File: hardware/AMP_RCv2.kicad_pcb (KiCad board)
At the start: 2 copper layers, 100 x 85 mm, 47 parts, among them CN3 Conn_01x15, CN4 Conn_01x15, J1 USB_C_Receptacle_USB2.0_16P, SW1 SW_UP, SW2 SW_LEFT, SW3 SW_DOWN, SW4 SW_RIGHT, SW5 ON/OFF, U1 TPS61023, U2 MCP73831-2-OT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

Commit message: Finish routing
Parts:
- removed CN3, CN4: Conn_01x15, Connector_PinHeader_2.54mm:PinHeader_1x15_P2.54mm_Vertical
- added U7: NUCLEO32-F303K8, AMP_Custom:NUCLEO32, F.Cu at (145.7, 76.3)
- moved C8 142.7 mm to (167.0, 57.5), turned to 90 degrees
- moved C11 142.2 mm to (179.3, 69.5), turned to -90 degrees
- moved C12 129.8 mm to (174.8, 95.9), turned to -90 degrees
- moved C9 126.0 mm to (160.9, 63.0), turned to 180 degrees
- moved R9 124.6 mm to (181.5, 69.5), turned to -90 degrees
- moved C10 124.3 mm to (167.2, 84.3), turned to -90 degrees
- moved R6 112.8 mm to (169.2, 57.5), turned to 90 degrees
- moved R10 106.5 mm to (177.0, 95.9), turned to -90 degrees
- moved R7 97.6 mm to (160.9, 65.2), turned to 180 degrees
- moved L1 95.1 mm to (126.6, 121.0)
- moved R8 92.1 mm to (169.4, 84.3), turned to -90 degrees
- moved C4 90.7 mm to (128.7, 110.9), turned to 180 degrees
- moved C3 89.6 mm to (128.7, 113.1), turned to 180 degrees
- moved BT1 88.0 mm to (120.1, 131.2), turned to 0 degrees
- moved C7 86.0 mm to (116.0, 80.0), turned to -90 degrees
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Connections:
- net /PA7 renamed /SPI1_MOSI
- net /PB3 renamed /SPI1_SCK
- U5 pad 2: /PA6 -> /SPI1_MISO
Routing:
- net +3V3: track 0.00 -> 146.4 mm
- net /VBAT: track 0.00 -> 90.8 mm
- net /SPI1_SCK: track 0.00 -> 68.7 mm, vias 0 -> 3
- net +5V: track 0.00 -> 66.7 mm, vias 0 -> 2
- net /BAT_CHRG_STAT: track 0.00 -> 65.3 mm, vias 0 -> 6
- net /SPI1_MOSI: track 0.00 -> 64.4 mm, vias 0 -> 5
- net Net-(SW5-A): track 0.00 -> 60.3 mm
- net /JOYSTICK_RIGHT_H: track 0.00 -> 57.5 mm
- net /JOYSTICK_LEFT_V: track 0.00 -> 57.1 mm, vias 0 -> 4
- net /JOYSTICK_LEFT_H: track 0.00 -> 49.9 mm, vias 0 -> 4
- net GND: track 0.00 -> 47.3 mm, vias 0 -> 19
- net /JOYSTICK_RIGHT_V: track 0.00 -> 44.8 mm
- net /JOYSTICK_RIGHT_SW: track 0.00 -> 43.7 mm, vias 0 -> 4
- net /BUTTON_UP: track 0.00 -> 38.1 mm, vias 0 -> 2
- net /BUTTON_LEFT: track 0.00 -> 35.1 mm, vias 0 -> 2
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- added copper zone on B.Cu, net GND

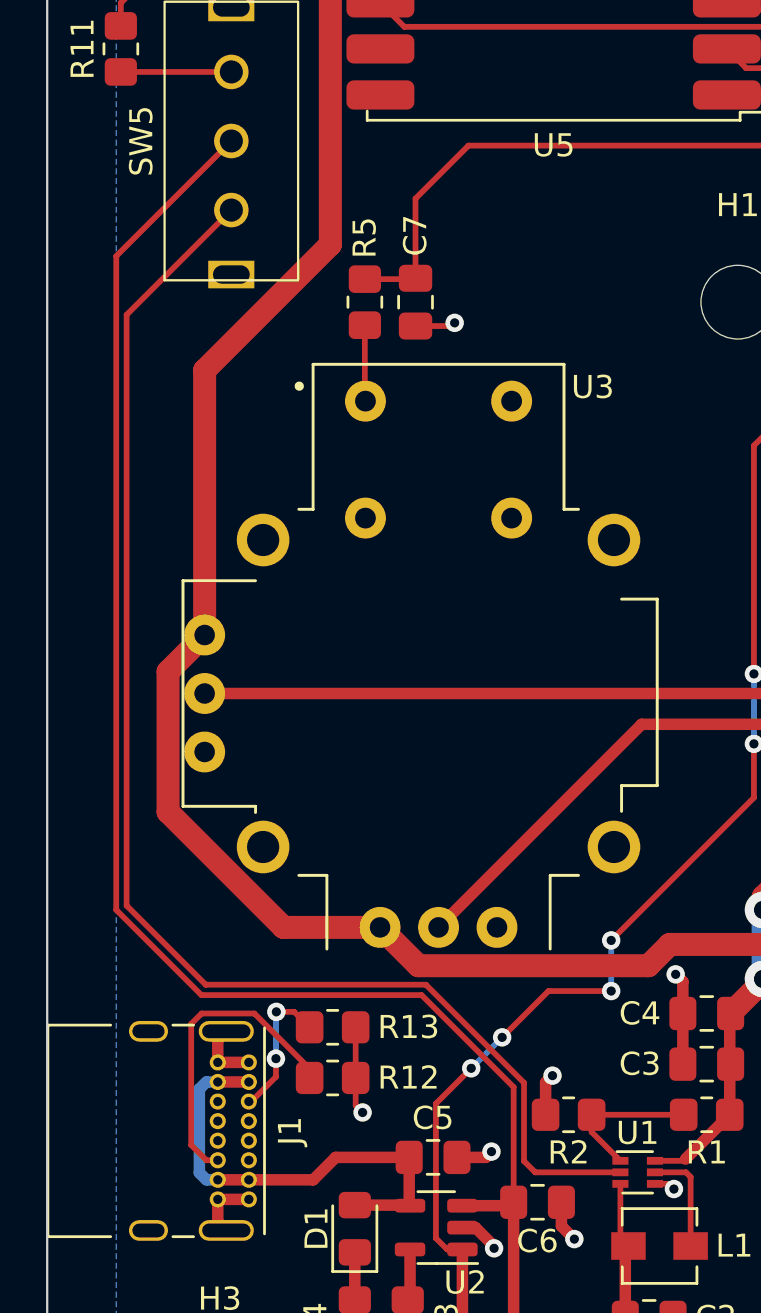
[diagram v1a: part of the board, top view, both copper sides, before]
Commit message: Fix incorrect power switch wiring
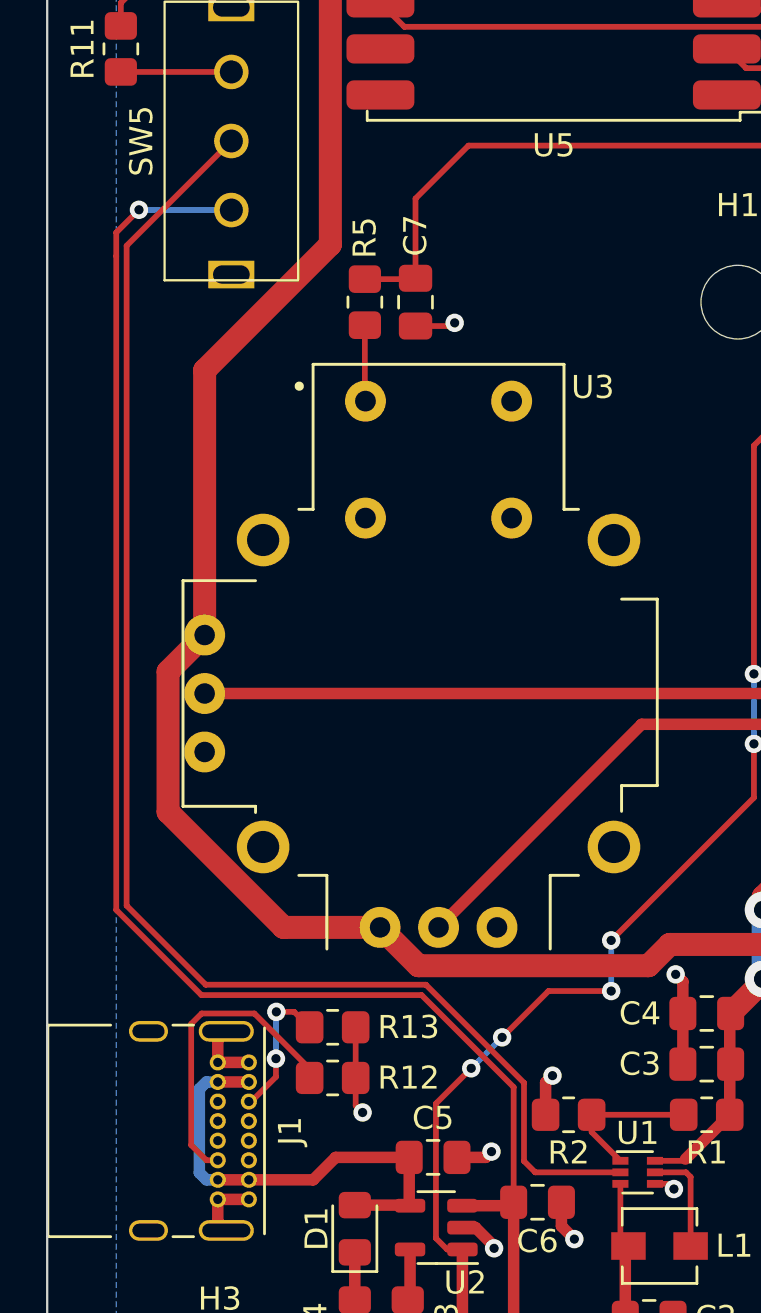
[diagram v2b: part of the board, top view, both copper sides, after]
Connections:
- SW5 pad 1: Net-(SW5-A) -> /VBAT
- SW5 pad 2: /VBAT -> Net-(SW5-B)
- U1 pad 2: Net-(SW5-A) -> Net-(SW5-B)
- U7 pad 28: unconnected-(U7-NRST-Pad28) -> unconnected-(U7-NRST-Pad28)_0
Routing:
- net Net-(SW5-B): track 0.00 -> 63.3 mm
- net Net-(SW5-A): track 60.3 -> 0.00 mm
- net /VBAT: track 90.8 -> 90.1 mm, vias 0 -> 1

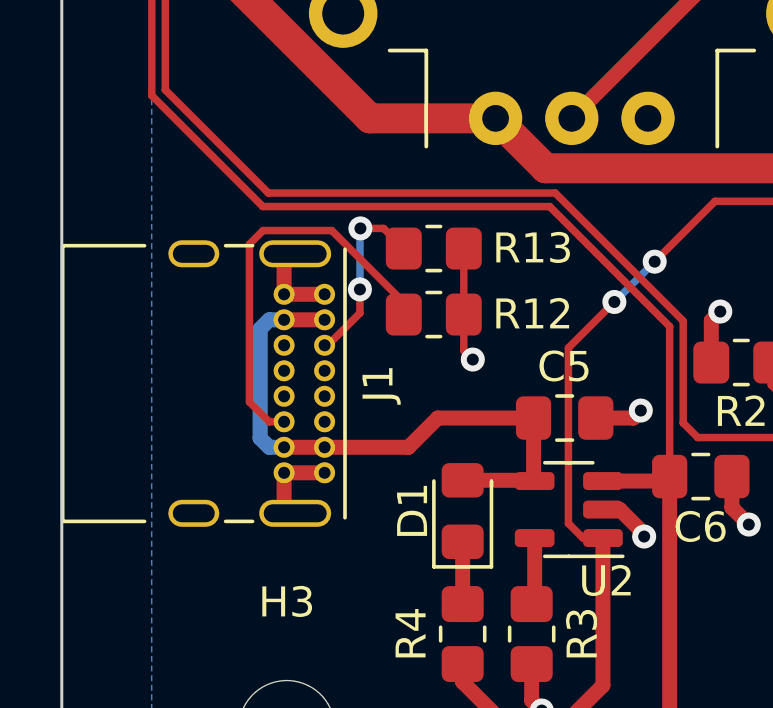
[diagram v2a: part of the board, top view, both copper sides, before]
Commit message: Replace USB-C port
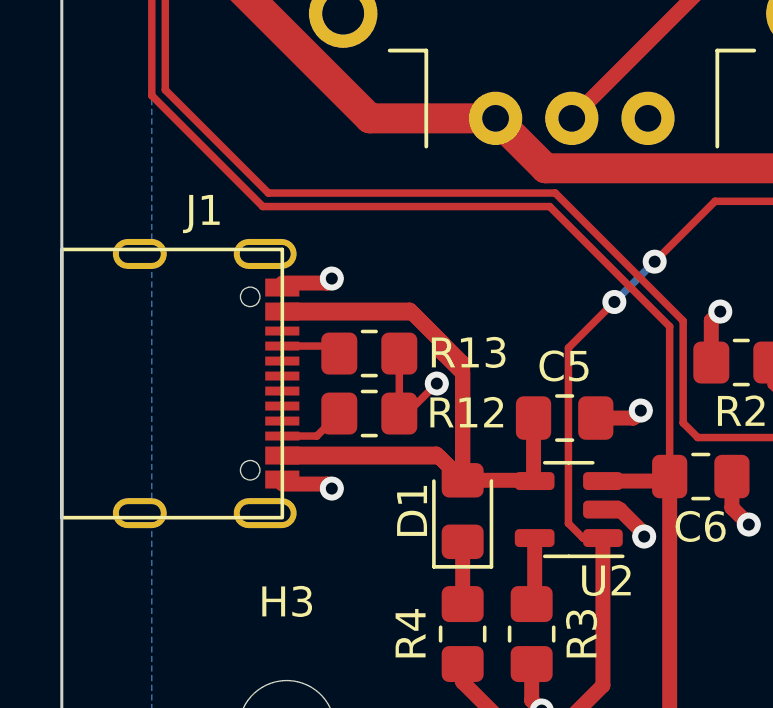
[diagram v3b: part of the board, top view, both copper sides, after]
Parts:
- J1: footprint Connector_USB:USB_C_Receptacle_GCT_USB4085 -> AMP_Custom:USB_C_Receptacle_Amphenol_C12402012
- moved J1 6.31 mm to (102.6, 111.7)
- moved R13 4.11 mm to (110.2, 115.0)
- moved R12 3.94 mm to (110.2, 117.0)
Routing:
- net VBUS: track 20.1 -> 38.4 mm
- net Net-(J1-CC2): track 13.4 -> 2.21 mm
- net Net-(J1-CC1): track 6.18 -> 2.00 mm, vias 2 -> 0
- net GND: track 47.3 -> 44.8 mm, vias 19 -> 21
